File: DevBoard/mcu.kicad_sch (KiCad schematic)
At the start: 45 parts, among them J301 SWD, J302 UART debug, J303 Spare GPIO, SW301 RESET, U301 STM32WB1MMC

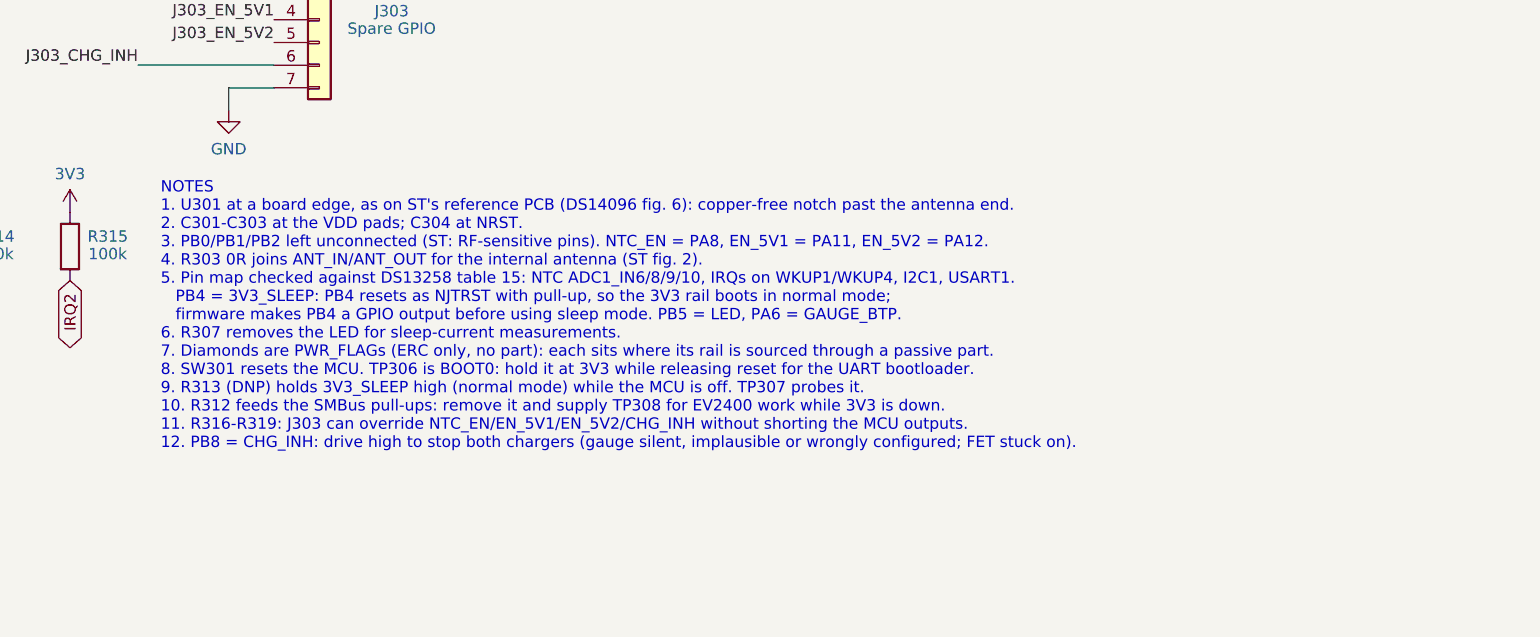
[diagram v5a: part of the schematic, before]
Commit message: Dev board rev A5: FET ESD caps, review 2, fail-safe CHG_INH, MCU I/O plan
- Gauge: C110/C111 (2 x 0.1 uF in series) across the protection FET pair,
  TI BQ40Z50-R2 fig. 9-2 C1/C2; C107/C108 across PACK+/PACK- unchanged.
- Second 3-reviewer schematic review with a challenge round
  (docs/devboard/schematic-review-2-2026-10-12.md, raw files in review2/):
  0 critical, 1 major (gauge precharge config), hardware proposals listed.
- CHG_INH now fails safe: R417/R517 47k pull-up on CE to 3V3; the MCU
  drives PB8 low to allow charging. MCU IWDG in hardware mode.
- Decisions: ICHG stays 9.1k; F101 stays 15 A with a gauge cut-off of
  2.8 V/cell or higher under load.
- docs/devboard/mcu-io-power-states.md: every MCU pin per power state,
  reconciled with the 150 uA sleep budget (PB8 low only while charging).

Co-Authored-By: Claude Opus 5.5 <noreply@anthropic.com>
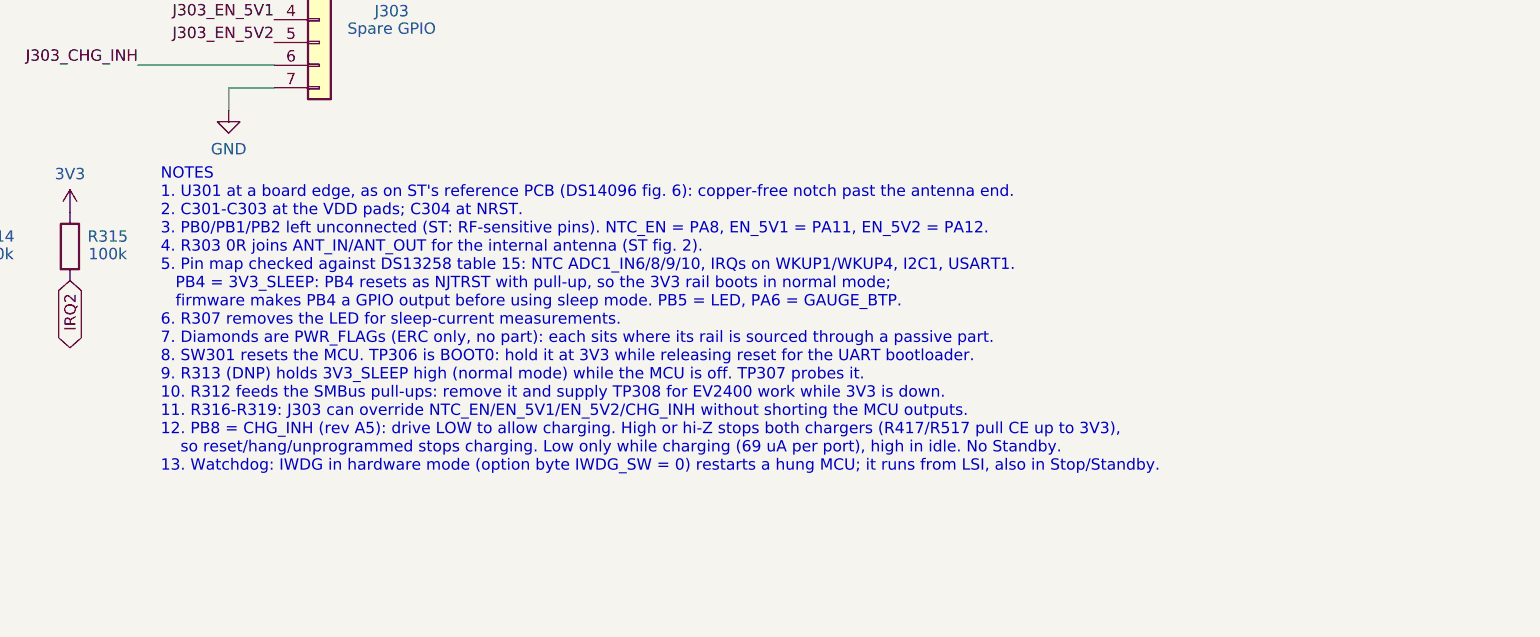
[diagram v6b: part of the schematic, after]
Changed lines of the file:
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@@
 		)
 	)
-	(text "NOTES\n1. U301 at a board edge, as on ST's reference PCB (DS14096 fig. 6): copper-free notch past the antenna end.\n2. C301-C303 at the VDD pads; C304 at NRST.\n3. PB0/PB1/PB2 left unconnected (ST: RF-sensitive pins). NTC_EN = PA8, EN_5V1 = PA11, EN_5V2 = PA12.\n4. R303 0R joins ANT_IN/ANT_OUT for the internal antenna (ST fig. 2).\n5. Pin map checked against DS13258 table 15: NTC ADC1_IN6/8/9/10, IRQs on WKUP1/WKUP4, I2C1, USART1.\n   PB4 = 3V3_SLEEP: PB4 resets as NJTRST with pull-up, so the 3V3 rail boots in normal mode;\n   firmware makes PB4 a GPIO output before using sleep mode. PB5 = LED, PA6 = GAUGE_BTP.\n6. R307 removes the LED for sleep-current measurements.\n7. Diamonds are PWR_FLAGs (ERC only, no part): each sits where its rail is sourced through a passive part.\n8. SW301 resets the MCU. TP306 is BOOT0: hold it at 3V3 while releasing reset for the UART bootloader.\n9. R313 (DNP) holds 3V3_SLEEP high (normal mode) while the MCU is off. TP307 probes it.\n10. R312 feeds the SMBus pull-ups: remove it and supply TP308 for EV2400 work while 3V3 is down.\n11. R316-R319: J303 can override NTC_EN/EN_5V1/EN_5V2/CHG_INH without shorting the MCU outputs.\n12. PB8 = CHG_INH: drive high to stop both chargers (gauge silent, implausible or wrongly configured; FET stuck on)."
+	(text "NOTES\n1. U301 at a board edge, as on ST's reference PCB (DS14096 fig. 6): copper-free notch past the antenna end.\n2. C301-C303 at the VDD pads; C304 at NRST.\n3. PB0/PB1/PB2 left unconnected (ST: RF-sensitive pins). NTC_EN = PA8, EN_5V1 = PA11, EN_5V2 = PA12.\n4. R303 0R joins ANT_IN/ANT_OUT for the internal antenna (ST fig. 2).\n5. Pin map checked against DS13258 table 15: NTC ADC1_IN6/8/9/10, IRQs on WKUP1/WKUP4, I2C1, USART1.\n   PB4 = 3V3_SLEEP: PB4 resets as NJTRST with pull-up, so the 3V3 rail boots in normal mode;\n   firmware makes PB4 a GPIO output before using sleep mode. PB5 = LED, PA6 = GAUGE_BTP.\n6. R307 removes the LED for sleep-current measurements.\n7. Diamonds are PWR_FLAGs (ERC only, no part): each sits where its rail is sourced through a passive part.\n8. SW301 resets the MCU. TP306 is BOOT0: hold it at 3V3 while releasing reset for the UART bootloader.\n9. R313 (DNP) holds 3V3_SLEEP high (normal mode) while the MCU is off. TP307 probes it.\n10. R312 feeds the SMBus pull-ups: remove it and supply TP308 for EV2400 work while 3V3 is down.\n11. R316-R319: J303 can override NTC_EN/EN_5V1/EN_5V2/CHG_INH without shorting the MCU outputs.\n12. PB8 = CHG_INH (rev A5): drive LOW to allow charging. High or hi-Z stops both chargers (R417/R517 pull CE up to 3V3),\n    so reset/hang/unprogrammed stops charging. Low only while charging (69 uA per port), high in idle. No Standby.\n13. Watchdog: IWDG in hardware mode (option byte IWDG_SW = 0) restarts a hung MCU; it runs from LSI, also in Stop/Standby."
 		(exclude_from_sim no)
-		(at 287.02 213.36 0)
+		(at 287.02 215.9 0)
 		(effects
 			(font

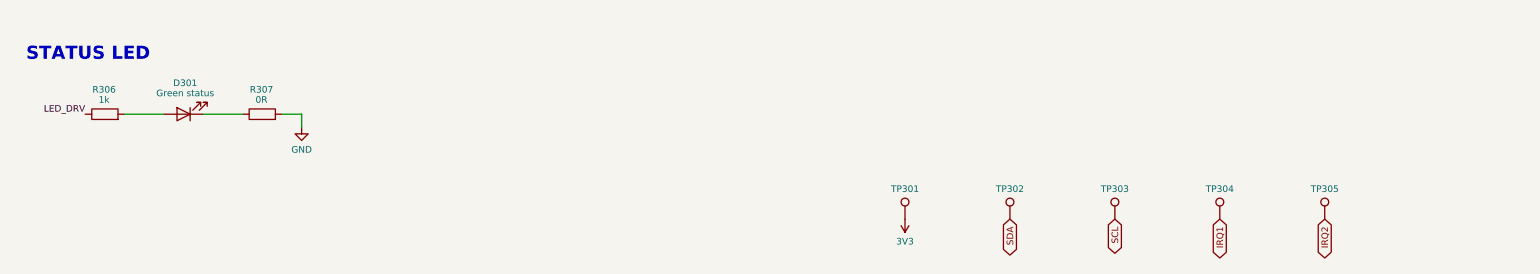
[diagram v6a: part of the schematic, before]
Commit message: Dev board rev A5: BAT fed before F101, review 2 hardware fixes, JLC passives
- Gauge BAT feed follows TI fig. 9-12: D101 from the cell top (CELL_P_RAW)
  before F101, so the gauge stays powered if the fuse opens or is unfitted.
- C421/C521 100 uF 35 V polymer (same 6.3 mm footprint): about 99 uF worst
  case vs the BQ25756 80 uF minimum after derating.
- Bootstrap diodes LRB520S-40T1G, Q103 BSS138, DNP C109 4.7 nF (fit D103
  with it), PPHV 0.1 uF and VBUS 10 nF per port, R306 330R, C201 DNP flag.
- Test points: GND loops by each port's SW probes and in the pack probe
  field, CELL_P_RAW, CE_N, LDO_3V3, LDO_IN, 5V_AMP.
- JLC part numbers on every resistor and capacitor.
- Placement for the new parts; placer hides test-point labels with no
  free spot. DRC clean, schematic parity clean.

Co-Authored-By: Claude Opus 5.5 <noreply@anthropic.com>
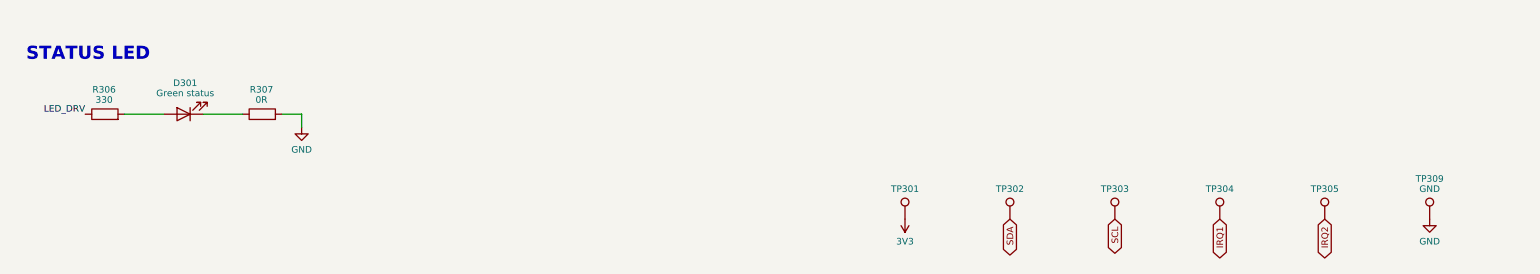
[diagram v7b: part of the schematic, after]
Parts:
- added TP309: GND, TestPoint:TestPoint_Keystone_5000-5004_Miniature, symbol Connector:TestPoint
- R301: LCSC (none) -> C17477; MPN (none) -> 0805W8F0000T5E
- R302: LCSC (none) -> C25804; MPN (none) -> 0603WAF1002T5E
- R303: LCSC (none) -> C17168; MPN (none) -> 0402WGF0000TCE
- R304, R305: LCSC (none) -> C23162; MPN (none) -> 0603WAF4701T5E
- R306: value 1k -> 330; LCSC (none) -> C23138; MPN (none) -> 0603WAF3300T5E; Notes (none) -> InGaN green (Vf ~3 V): 330R gives ~1 mA from 3.3 V (1k gave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
- R307: LCSC (none) -> C21189; MPN (none) -> 0603WAF0000T5E
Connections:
- net GND: now also TP309.1

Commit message: Dev board: SMD test loops (RH-S2761-46R) instead of Keystone through-hole
All 45 loop test points become ronghe RH-S2761-46R (LCSC C55121754), the
JLC-stocked equivalent of the Harwin S2761-46R: 1.6 x 0.8 x 1.15 mm SMT
loop on an 0603 land pattern, 3.5 A. New footprint
MonolithDev:TestPoint_Harwin_S2761_0603 (make_footprints.py section 11),
both pads pin 1 and jumpered. JLC places them; no through-hole assembly.

Co-Authored-By: Claude Opus 5.5 <noreply@anthropic.com>
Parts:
- TP301, TP302, TP303, TP304, TP305, TP308, TP309: footprint TestPoint:TestPoint_Keystone_5000-5004_Miniature -> MonolithDev:TestPoint_Harwin_S2761_0603; LCSC (none) -> C55121754; MPN (none) -> RH-S2761-46R (ronghe; Harwin S2761-46R equivalent)
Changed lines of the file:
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@@
 			)
 		)
-		(property "Footprint" "TestPoint:TestPoint_Keystone_5000-5004_Miniature"
+		(property "Footprint" "MonolithDev:TestPoint_Harwin_S2761_0603"
 			(at 236.22 264.16 0)
 			(hide yes)
@@
 			)
 		)
+		(property "LCSC" "C55121754"
+			(at 231.14 264.16 0)
+			(hide yes)
+			(show_name no)
+			(do_not_autoplace no)
+			(effects
+				(font
+					(size 1.27 1.27)
+				)
+			)
+		)
+		(property "MPN" "RH-S2761-46R (ronghe; Harwin S2761-46R equivalent)"
+			(at 231.14 264.16 0)
+			(hide yes)
+			(show_name no)
+			(do_not_autoplace no)
+			(effects
+				(font
+					(size 1.27 1.27)
+				)
+			)
+		)
 		(pin "1"
 		)
@@
 			)
 		)
-		(property "Footprint" "TestPoint:TestPoint_Keystone_5000-5004_Miniature"
+		(property "Footprint" "MonolithDev:TestPoint_Harwin_S2761_0603"
 			(at 276.86 264.16 0)
 			(hide yes)
@@
 			)
 		)
+		(property "LCSC" "C55121754"
+			(at 271.78 264.16 0)
+			(hide yes)
+			(show_name no)
+			(do_not_autoplace no)
+			(effects
+				(font
+					(size 1.27 1.27)
+				)
+			)
+		)
+		(property "MPN" "RH-S2761-46R (ronghe; Harwin S2761-46R equivalent)"
+			(at 271.78 264.16 0)
+			(hide yes)
+			(show_name no)
+			(do_not_autoplace no)
+			(effects
+				(font
+					(size 1.27 1.27)
+				)
+			)
+		)
 		(pin "1"
 		)
@@
 			)
 		)
-		(property "Footprint" "TestPoint:TestPoint_Keystone_5000-5004_Miniature"
+		(property "Footprint" "MonolithDev:TestPoint_Harwin_S2761_0603"
 			(at 215.9 264.16 0)
 			(hide yes)
@@
 			)
 		)
+		(property "LCSC" "C55121754"
+			(at 210.82 264.16 0)
+			(hide yes)
+			(show_name no)
+			(do_not_autoplace no)
+			(effects
+				(font
+					(size 1.27 1.27)
+				)
+			)
+		)
+		(property "MPN" "RH-S2761-46R (ronghe; Harwin S2761-46R equivalent)"
+			(at 210.82 264.16 0)
+			(hide yes)
+			(show_name no)
+			(do_not_autoplace no)
+			(effects
+				(font
+					(size 1.27 1.27)
+				)
+			)
+		)
 		(pin "1"
 		)
@@
 			)
 		)
-		(property "Footprint" "TestPoint:TestPoint_Keystone_5000-5004_Miniature"
+		(property "Footprint" "MonolithDev:TestPoint_Harwin_S2761_0603"
 			(at 256.54 264.16 0)
 			(hide yes)
@@
 			)
 		)
+		(property "LCSC" "C55121754"
+			(at 251.46 264.16 0)
+			(hide yes)
+			(show_name no)
+			(do_not_autoplace no)
+			(effects
+				(font
+					(size 1.27 1.27)
+				)
+			)
+		)
+		(property "MPN" "RH-S2761-46R (ronghe; Harwin S2761-46R equivalent)"
+			(at 251.46 264.16 0)
+			(hide yes)
+			(show_name no)
+			(do_not_autoplace no)
+			(effects
+				(font
+					(size 1.27 1.27)
+				)
+			)
+		)
 		(pin "1"
 		)
@@
 			)
 		)
-		(property "Footprint" "TestPoint:TestPoint_Keystone_5000-5004_Miniature"
+		(property "Footprint" "MonolithDev:TestPoint_Harwin_S2761_0603"
 			(at 297.18 264.16 0)
 			(hide yes)
@@
 			)
 		)
+		(property "LCSC" "C55121754"
+			(at 292.1 264.16 0)
+			(hide yes)
+			(show_name no)
+			(do_not_autoplace no)
+			(effects
+				(font
+					(size 1.27 1.27)
+				)
+			)
+		)
+		(property "MPN" "RH-S2761-46R (ronghe; Harwin S2761-46R equivalent)"
+			(at 292.1 264.16 0)
+			(hide yes)
+			(show_name no)
+			(do_not_autoplace no)
+			(effects
+				(font
+					(size 1.27 1.27)
+				)
+			)
+		)
 		(pin "1"
 		)
@@
 			)
 		)
-		(property "Footprint" "TestPoint:TestPoint_Keystone_5000-5004_Miniature"
+		(property "Footprint" "MonolithDev:TestPoint_Harwin_S2761_0603"
 			(at 223.52 193.04 0)
 			(hide yes)
@@
 			)
 		)
+		(property "LCSC" "C55121754"
+			(at 223.52 193.04 0)
+			(hide yes)
+			(show_name no)
+			(do_not_autoplace no)
+			(effects
+				(font
+					(size 1.27 1.27)
+				)
+			)
+		)
+		(property "MPN" "RH-S2761-46R (ronghe; Harwin S2761-46R equivalent)"
+			(at 223.52 193.04 0)
+			(hide yes)
+			(show_name no)
+			(do_not_autoplace no)
+			(effects
+				(font
+					(size 1.27 1.27)
+				)
+			)
+		)
 		(pin "1"
 		)
@@
 			)
 		)
-		(property "Footprint" "TestPoint:TestPoint_Keystone_5000-5004_Miniature"
+		(property "Footprint" "MonolithDev:TestPoint_Harwin_S2761_0603"
 			(at 312.42 264.16 0)
 			(hide yes)
@@
 			(at 312.42 264.16 0)
 			(hide yes)
+			(show_name no)
+			(do_not_autoplace no)
+			(effects
+				(font
+					(size 1.27 1.27)
+				)
+			)
+		)
+		(property "LCSC" "C55121754"
+			(at 312.42 264.16 0)
+			(hide yes)
+			(show_name no)
+			(do_not_autoplace no)
+			(effects
+				(font
+					(size 1.27 1.27)
+				)
+			)
+		)
+		(property "MPN" "RH-S2761-46R (ronghe; Harwin S2761-46R equivalent)"
+			(at 312.42 264.16 0)
+			(hide yes)
